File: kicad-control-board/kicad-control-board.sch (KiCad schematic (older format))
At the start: 99 parts, among them J1 Conn_01x10_Female, J2 Conn_01x15_Male, J3 BA56_3DIG_7SEG, J4 Gate Out, J5 Clock Out, J6 Clock In, J7 Pitch Out, J8 CV Out, J9 Reset In, Q1 2N3904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

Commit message: Kicad cache
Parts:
- RV1, RV2, RV3, RV4: symbol Device:POT -> kicad-control-board-rescue:POT-Device
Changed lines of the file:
@@
 EESchema Schematic File Version 4
 LIBS:kicad-control-board-cache
-EELAYER 26 0
+EELAYER 29 0
 EELAYER END
 $Descr A4 11693 8268
@@
 $EndComp
 $Comp
-L Device:POT RV2
+L kicad-control-board-rescue:POT-Device RV2
 U 1 1 5B32F1D2
 P 10550 5350
@@
 $EndComp
 $Comp
-L Device:POT RV3
+L kicad-control-board-rescue:POT-Device RV3
 U 1 1 5B32F556
 P 10550 5750
@@
 $EndComp
 $Comp
-L Device:POT RV4
+L kicad-control-board-rescue:POT-Device RV4
 U 1 1 5B32F5FF
 P 10550 6150
@@
 $EndComp
 $Comp
-L Device:POT RV1
+L kicad-control-board-rescue:POT-Device RV1
 U 1 1 5B32F113
 P 10550 4950

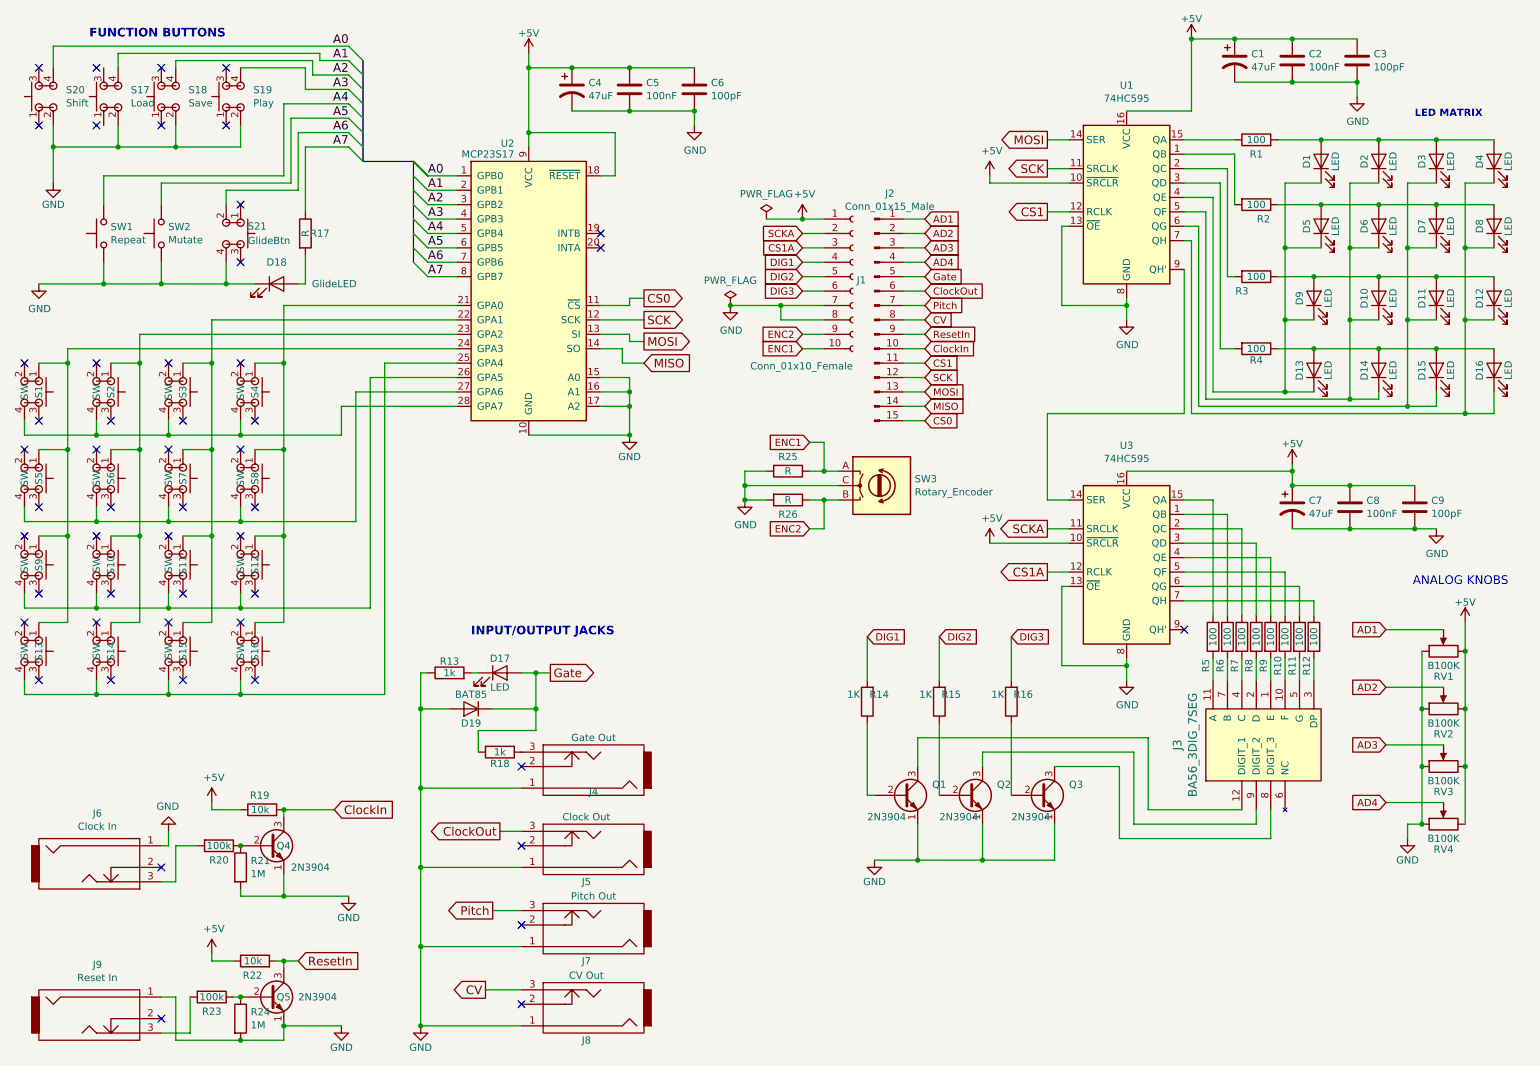
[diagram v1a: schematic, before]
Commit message: Updating PCB and schematics for assembly bugfixes
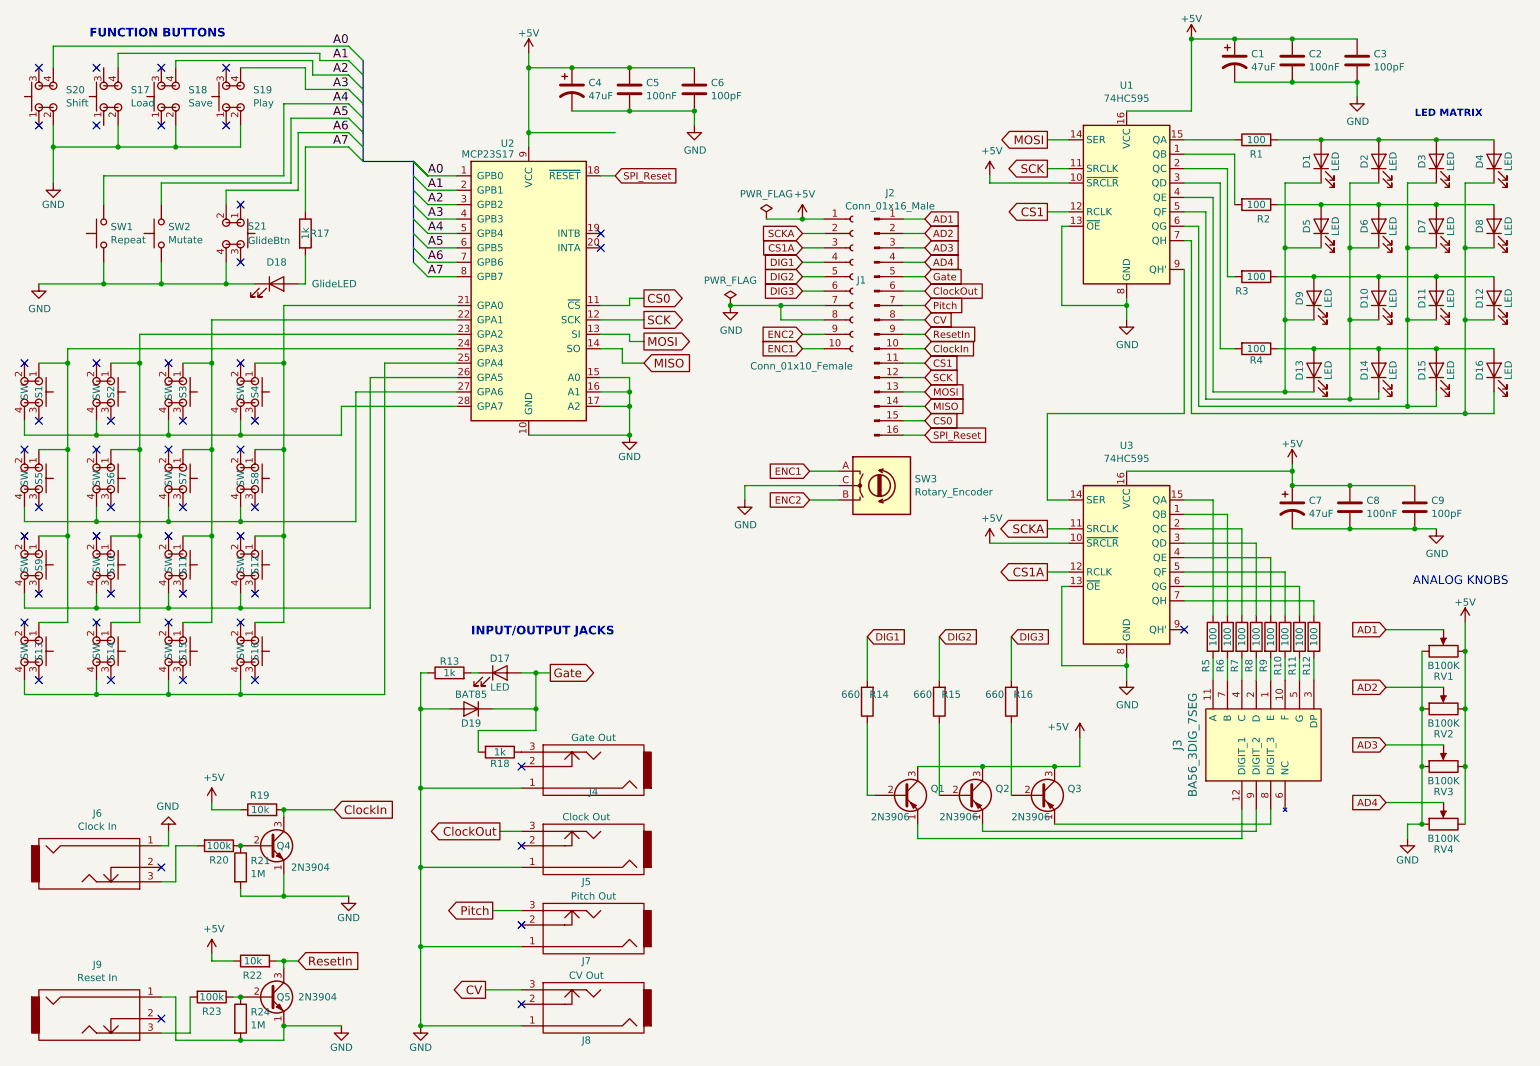
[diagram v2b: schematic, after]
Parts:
- removed J2: Conn_01x15_Male, Pin_Headers:Pin_Header_Straight_1x15_Pitch2.54mm, symbol Connector:Conn_01x15_Male
- removed Q1, Q2, Q3: 2N3904, TO_SOT_Packages_THT:TO-92_Inline_Narrow_Oval, symbol Transistor_BJT:2N3904
- removed R25, R26: R, Resistors_THT:R_Axial_DIN0204_L3.6mm_D1.6mm_P7.62mm_Horizontal, symbol Device:R
- added J2: Conn_01x16_Male, Pin_Headers:Pin_Header_Straight_1x16_Pitch2.54mm, symbol Connector:Conn_01x16_Male
- added Q1, Q2, Q3: 2N3906, TO_SOT_Packages_THT:TO-92_Inline_Wide, symbol Transistor_BJT:2N3906
- C3, C6, C9: footprint Capacitors_THT:C_Disc_D3.8mm_W2.6mm_P2.50mm -> Capacitors_THT:C_Disc_D5.0mm_W2.5mm_P2.50mm
- Q4, Q5: footprint TO_SOT_Packages_THT:TO-92_Inline_Narrow_Oval -> TO_SOT_Packages_THT:TO-92_Inline_Wide
- R14, R15, R16: value 1K -> 660
- R17: value R -> 1k
- RV1, RV2, RV3, RV4: footprint Eurocad:Alpha9mmPot -> Potentiometers:Potentiometer_Alps_RK09K_Horizontal
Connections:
- net +5V: now also Q1.3 (C), Q2.3 (C), Q3.3 (C); no longer U2.18 (~RESET)
- net AD1: now also J2.1 (Pin_1)
- net AD2: now also J2.2 (Pin_2)
- net AD3: now also J2.3 (Pin_3)
- net AD4: now also J2.4 (Pin_4)
- net CS0: now also J2.15 (Pin_15)
- net CS1: now also J2.11 (Pin_11)
- net CV: now also J2.8 (Pin_8)
- net ClockIn: now also J2.10 (Pin_10)
- net ClockOut: now also J2.6 (Pin_6)
- net Gate: now also J2.5 (Pin_5)
- net MISO: now also J2.14 (Pin_14)
- net MOSI: now also J2.13 (Pin_13)
- net Pitch: now also J2.7 (Pin_7)
- net ResetIn: now also J2.9 (Pin_9)
- net SCK: now also J2.12 (Pin_12)
- net at R16.1: now also Q3.2 (B)
- net at J3.8 (DIGIT_3): now also Q3.1 (E)
- net at R15.1: now also Q2.2 (B)
- net at J3.9 (DIGIT_2): now also Q2.1 (E)
- net at R14.1: now also Q1.2 (B)
- net at J3.12 (DIGIT_1): now also Q1.1 (E)
- new net SPI_Reset: J2.16 (Pin_16), U2.18 (~RESET)

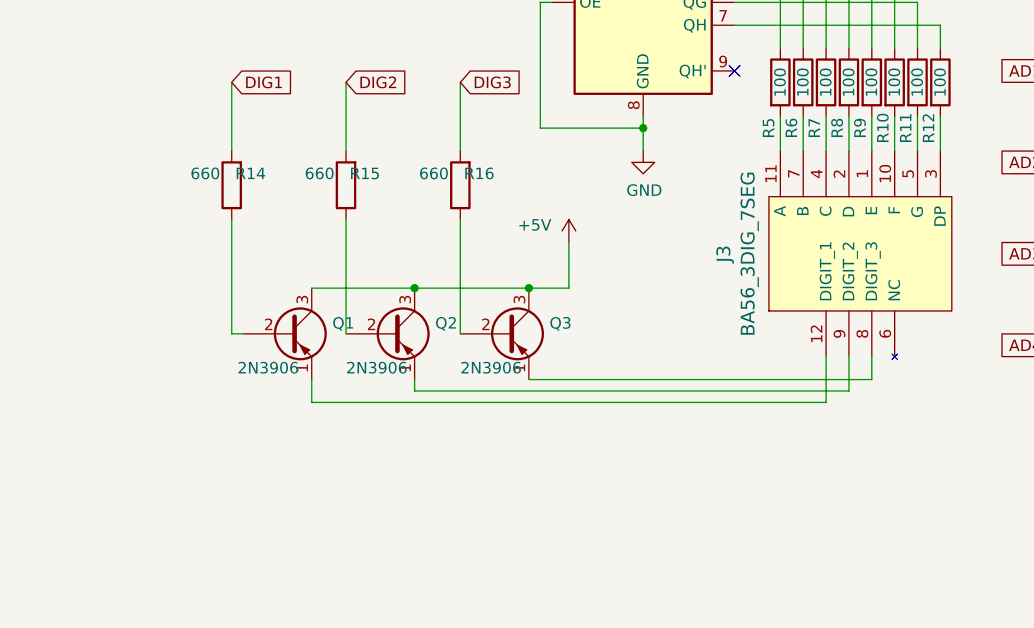
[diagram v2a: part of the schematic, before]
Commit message: Flipping 2n3906 transistors silkscreen
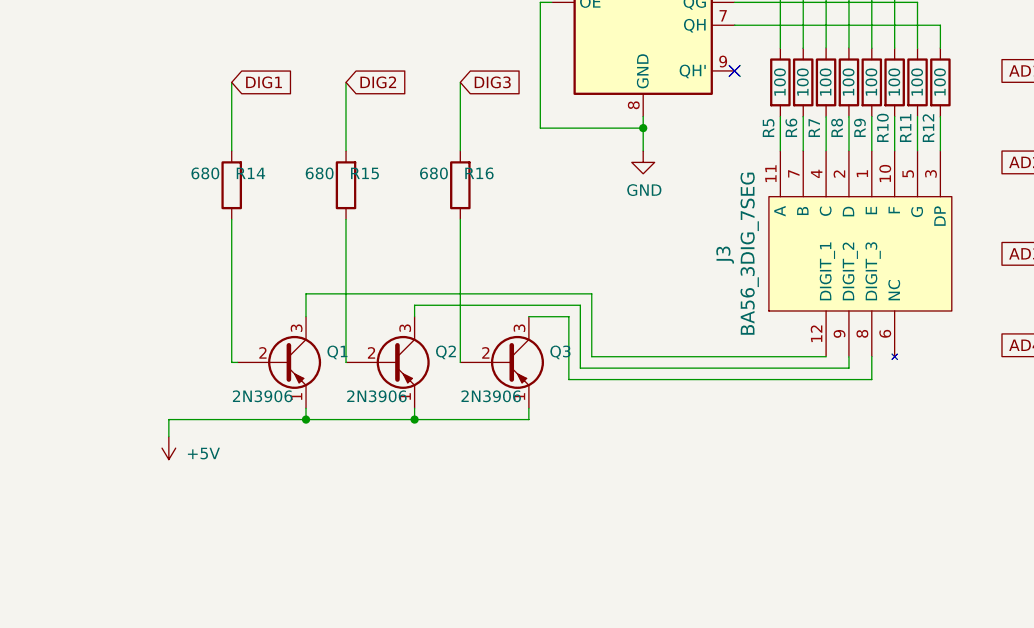
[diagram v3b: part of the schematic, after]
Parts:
- R14, R15, R16: value 660 -> 680
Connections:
- net +5V: now also Q1.1 (E), Q2.1 (E), Q3.1 (E); no longer Q1.3 (C), Q2.3 (C), Q3.3 (C)
- net at J3.12 (DIGIT_1): now also Q1.3 (C); no longer Q1.1 (E)
- net at J3.9 (DIGIT_2): now also Q2.3 (C); no longer Q2.1 (E)
- net at J3.8 (DIGIT_3): now also Q3.3 (C); no longer Q3.1 (E)
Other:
- moved on the sheet: Q1, Q2, Q3
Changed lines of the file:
@@
 P 6550 5300
 F 0 "R14" H 6400 5250 50  0000 L CNN
-F 1 "660" H 6600 5250 50  0000 L CNN
+F 1 "680" H 6600 5250 50  0000 L CNN
 F 2 "Resistors_THT:R_Axial_DIN0204_L3.6mm_D1.6mm_P7.62mm_Horizontal" V 6480 5300 50  0001 C CNN
 F 3 "" H 6550 5300 50  0001 C CNN
@@
 P 7050 5300
 F 0 "R15" H 6900 5250 50  0000 L CNN
-F 1 "660" H 7100 5250 50  0000 L CNN
+F 1 "680" H 7100 5250 50  0000 L CNN
 F 2 "Resistors_THT:R_Axial_DIN0204_L3.6mm_D1.6mm_P7.62mm_Horizontal" V 6980 5300 50  0001 C CNN
 F 3 "" H 7050 5300 50  0001 C CNN
@@
 P 7550 5300
 F 0 "R16" H 7400 5250 50  0000 L CNN
-F 1 "660" H 7600 5250 50  0000 L CNN
+F 1 "680" H 7600 5250 50  0000 L CNN
 F 2 "Resistors_THT:R_Axial_DIN0204_L3.6mm_D1.6mm_P7.62mm_Horizontal" V 7480 5300 50  0001 C CNN
 F 3 "" H 7550 5300 50  0001 C CNN
@@
 	2950 1450 3050 1550
 Wire Wire Line
-	6550 5950 6600 5950
-Wire Wire Line
-	9350 6050 9350 6150
-Wire Wire Line
-	7050 5450 7050 5950
-Wire Wire Line
-	6550 5450 6550 5950
-Wire Wire Line
-	7550 5450 7550 5950
-Wire Wire Line
 	7800 3900 7950 3900
 Wire Wire Line
@@
 L Transistor_BJT:2N3906 Q1
 U 1 1 5DBBE59D
-P 6800 5950
-F 0 "Q1" H 6990 5996 50  0000 L CNN
-F 1 "2N3906" H 6575 5800 50  0000 L CNN
-F 2 "TO_SOT_Packages_THT:TO-92_Inline_Wide" H 7000 5875 50  0001 L CIN
-F 3 "https://www.fairchildsemi.com/datasheets/2N/2N3906.pdf" H 6800 5950 50  0001 L CNN
-	1    6800 5950
+P 6775 6075
+F 0 "Q1" H 6965 6121 50  0000 L CNN
+F 1 "2N3906" H 6550 5925 50  0000 L CNN
+F 2 "TO_SOT_Packages_THT:TO-92_Inline_Wide" H 6975 6000 50  0001 L CIN
+F 3 "https://www.fairchildsemi.com/datasheets/2N/2N3906.pdf" H 6775 6075 50  0001 L CNN
+	1    6775 6075
 	1    0    0    -1
 $EndComp
@@
 L Transistor_BJT:2N3906 Q2
 U 1 1 5DBC04EA
-P 7250 5950
-F 0 "Q2" H 7440 5996 50  0000 L CNN
-F 1 "2N3906" H 7050 5800 50  0000 L CNN
-F 2 "TO_SOT_Packages_THT:TO-92_Inline_Wide" H 7450 5875 50  0001 L CIN
-F 3 "https://www.fairchildsemi.com/datasheets/2N/2N3906.pdf" H 7250 5950 50  0001 L CNN
-	1    7250 5950
+P 7250 6075
+F 0 "Q2" H 7440 6121 50  0000 L CNN
+F 1 "2N3906" H 7050 5925 50  0000 L CNN
+F 2 "TO_SOT_Packages_THT:TO-92_Inline_Wide" H 7450 6000 50  0001 L CIN
+F 3 "https://www.fairchildsemi.com/datasheets/2N/2N3906.pdf" H 7250 6075 50  0001 L CNN
+	1    7250 6075
 	1    0    0    -1
 $EndComp
@@
 L Transistor_BJT:2N3906 Q3
 U 1 1 5DBC0DB5
-P 7750 5950
-F 0 "Q3" H 7940 5996 50  0000 L CNN
-F 1 "2N3906" H 7550 5800 50  0000 L CNN
-F 2 "TO_SOT_Packages_THT:TO-92_Inline_Wide" H 7950 5875 50  0001 L CIN
-F 3 "https://www.fairchildsemi.com/datasheets/2N/2N3906.pdf" H 7750 5950 50  0001 L CNN
-	1    7750 5950
-	1    0    0    -1
-$EndComp
-$Comp
-L power:+5V #PWR021
-U 1 1 5DC2EE30
-P 8025 5550
-F 0 "#PWR021" H 8025 5400 50  0001 C CNN
-F 1 "+5V" H 7875 5625 50  0000 C CNN
-F 2 "" H 8025 5550 50  0001 C CNN
-F 3 "" H 8025 5550 50  0001 C CNN
-	1    8025 5550
+P 7750 6075
+F 0 "Q3" H 7940 6121 50  0000 L CNN
+F 1 "2N3906" H 7550 5925 50  0000 L CNN
+F 2 "TO_SOT_Packages_THT:TO-92_Inline_Wide" H 7950 6000 50  0001 L CIN
+F 3 "https://www.fairchildsemi.com/datasheets/2N/2N3906.pdf" H 7750 6075 50  0001 L CNN
+	1    7750 6075
 	1    0    0    -1
 $EndComp
@@
 	6150 3700 6350 3700
 Wire Wire Line
-	6900 6250 6900 6150
-Wire Wire Line
 	6550 5150 6550 4850
 Text GLabel 7550 4850 2    50   Input ~ 0
@@
 Text GLabel 6550 4850 2    50   Input ~ 0
 DIG1
-Wire Wire Line
-	9150 6250 9150 6050
-Wire Wire Line
-	6900 6250 9150 6250
-Wire Wire Line
-	7350 6150 7350 6200
-Wire Wire Line
-	7350 6200 9250 6200
-Wire Wire Line
-	9250 6050 9250 6200
-Wire Wire Line
-	7850 6150 9350 6150
-Wire Wire Line
-	7850 5750 7350 5750
-Wire Wire Line
-	7350 5750 6900 5750
-Connection ~ 7350 5750
-Wire Wire Line
-	7850 5750 8025 5750
-Connection ~ 7850 5750
-Wire Wire Line
-	8025 5550 8025 5750
 $Comp
 L Connector:Conn_01x16_Male J2
@@
 Text GLabel 4800 1650 2    50   Input ~ 0
 SPI_Reset
+Wire Wire Line
+	6575 6075 6550 6075
+Wire Wire Line
+	6550 5450 6550 6075
+$Comp
+L power:+5V #PWR021
+U 1 1 5DC2EE30
+P 6275 6400
+F 0 "#PWR021" H 6275 6250 50  0001 C CNN
+F 1 "+5V" H 6125 6475 50  0000 C CNN
+F 2 "" H 6275 6400 50  0001 C CNN
+F 3 "" H 6275 6400 50  0001 C CNN
+	1    6275 6400
+	-1   0    0    1
+$EndComp
+Wire Wire Line
+	6275 6400 6275 6325
+Wire Wire Line
+	6275 6325 6875 6325
+Wire Wire Line
+	6875 6275 6875 6325
+Connection ~ 6875 6325
+Wire Wire Line
+	7050 6075 7050 5450
+Wire Wire Line
+	7550 5450 7550 6075
+Wire Wire Line
+	7850 6275 7850 6325
+Wire Wire Line
+	7350 6275 7350 6325
+Connection ~ 7350 6325
+Wire Wire Line
+	7350 6325 7850 6325
+Wire Wire Line
+	6875 6325 7350 6325
+Wire Wire Line
+	9150 6050 8125 6050
+Wire Wire Line
+	8125 6050 8125 5775
+Wire Wire Line
+	8125 5775 6875 5775
+Wire Wire Line
+	6875 5775 6875 5875
+Wire Wire Line
+	7350 5875 7350 5825
+Wire Wire Line
+	7350 5825 8075 5825
+Wire Wire Line
+	8075 5825 8075 6100
+Wire Wire Line
+	8075 6100 9250 6100
+Wire Wire Line
+	9250 6100 9250 6050
+Wire Wire Line
+	9350 6050 9350 6150
+Wire Wire Line
+	9350 6150 8025 6150
+Wire Wire Line
+	8025 6150 8025 5875
+Wire Wire Line
+	8025 5875 7850 5875
 Wire Bus Line
 	3050 850  3050 1550
